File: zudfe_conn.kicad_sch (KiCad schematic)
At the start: 5 parts, among them J1 6469028-1, J2 6469028-1, J3 6469028-1, J4 6469028-1, J5 6469028-1

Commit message: Finish Regulator section
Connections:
- net SFP4.TX_P: now reaches J1.A2
- net SFP5.TX_P: now reaches J1.A3
- net SFP6.TX_P: now reaches J1.A4
- net SFP7.TX_P: now reaches J1.A5
- net SFP4.TX_N: now reaches J1.B2
- net SFP5.TX_N: now reaches J1.B3
- net SFP6.TX_N: now reaches J1.B4
- net SFP7.TX_N: now reaches J1.B5
- net SFP4.RX_P: now reaches J1.C2
- net SFP5.RX_P: now reaches J1.C3
- net SFP6.RX_P: now reaches J1.C4
- net SFP7.RX_P: now reaches J1.C5
- net SFP4.RX_N: now reaches J1.D2
- net SFP5.RX_N: now reaches J1.D3
- net SFP6.RX_N: now reaches J1.D4
- net SFP7.RX_N: now reaches J1.D5
- net SFP0.TX_P: now reaches J3.A6
- net SFP1.TX_P: now reaches J3.A7
- net SFP2.TX_P: now reaches J3.A8
- net SFP3.TX_P: now reaches J3.A9
- net SFP0.TX_N: now reaches J3.B6
- net SFP1.TX_N: now reaches J3.B7
- net SFP2.TX_N: now reaches J3.B8
- net SFP3.TX_N: now reaches J3.B9
- net SFP0.RX_P: now reaches J3.C6
- net SFP1.RX_P: now reaches J3.C7
- net SFP2.RX_P: now reaches J3.C8
- net SFP3.RX_P: now reaches J3.C9
- net SFP0.RX_N: now reaches J3.D6
- net SFP1.RX_N: now reaches J3.D7
- net SFP2.RX_N: now reaches J3.D8
- net SFP3.RX_N: now reaches J3.D9

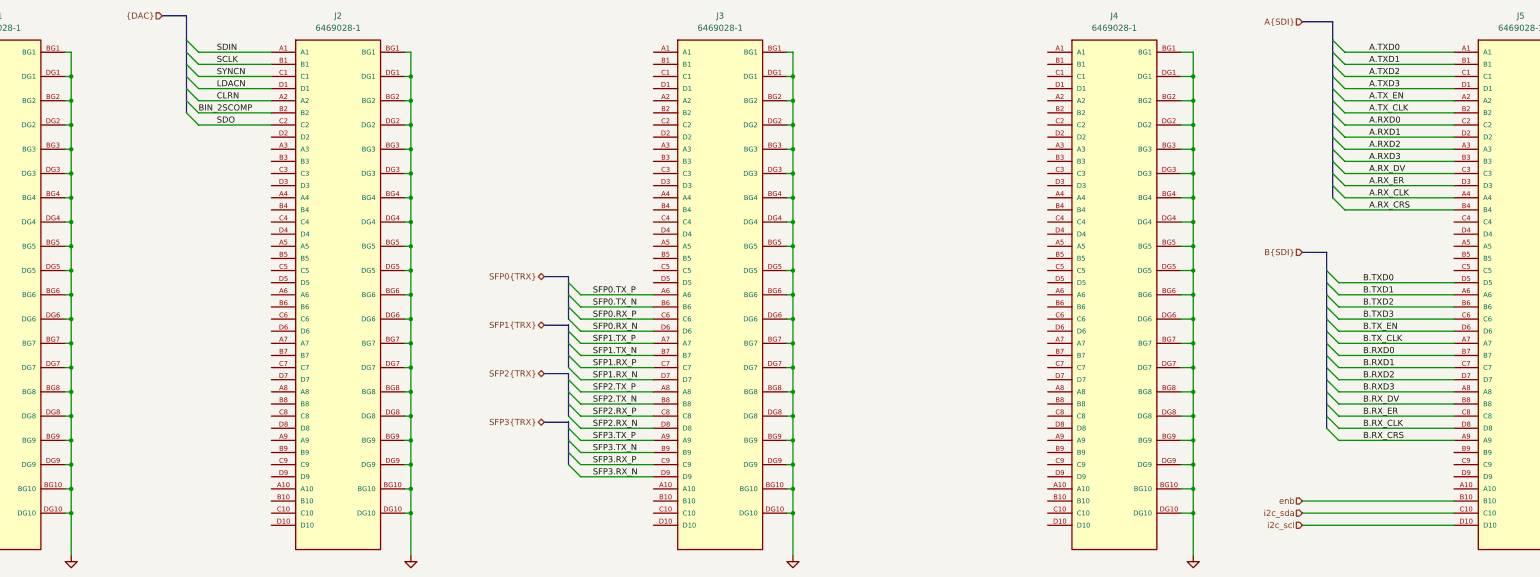
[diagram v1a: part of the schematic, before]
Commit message: Place SFP passives
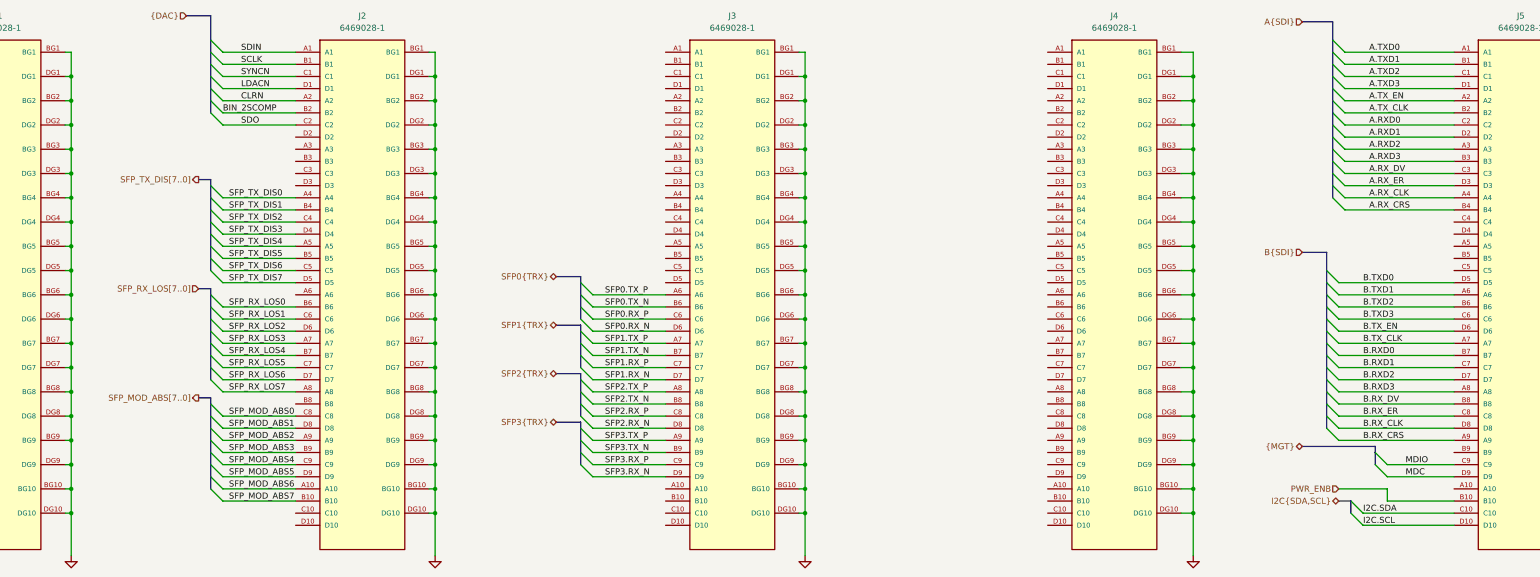
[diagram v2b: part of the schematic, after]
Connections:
- net SFP_MOD_ABS6: now reaches J2.A10
- net SFP_TX_DIS0: now reaches J2.A4
- net SFP_TX_DIS4: now reaches J2.A5
- net SFP_RX_LOS3: now reaches J2.A7
- net SFP_RX_LOS7: now reaches J2.A8
- net SFP_MOD_ABS2: now reaches J2.A9
- net SFP_MOD_ABS7: now reaches J2.B10
- net SFP_TX_DIS1: now reaches J2.B4
- net SFP_TX_DIS5: now reaches J2.B5
- net SFP_RX_LOS0: now reaches J2.B6
- net SFP_RX_LOS4: now reaches J2.B7
- net SFP_MOD_ABS3: now reaches J2.B9
- net SFP_TX_DIS2: now reaches J2.C4
- net SFP_TX_DIS6: now reaches J2.C5
- net SFP_RX_LOS1: now reaches J2.C6
- net SFP_RX_LOS5: now reaches J2.C7
- net SFP_MOD_ABS0: now reaches J2.C8
- net SFP_MOD_ABS4: now reaches J2.C9
- net SFP_TX_DIS3: now reaches J2.D4
- net SFP_TX_DIS7: now reaches J2.D5
- net SFP_RX_LOS2: now reaches J2.D6
- net SFP_RX_LOS6: now reaches J2.D7
- net SFP_MOD_ABS1: now reaches J2.D8
- net SFP_MOD_ABS5: now reaches J2.D9
- net MDIO: now reaches J5.C9
- net MDC: now reaches J5.D9
- net enb renamed PWR_ENB
- net i2c_scl renamed I2C.SCL
- net i2c_sda renamed I2C.SDA
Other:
- moved on the sheet: J2, J3

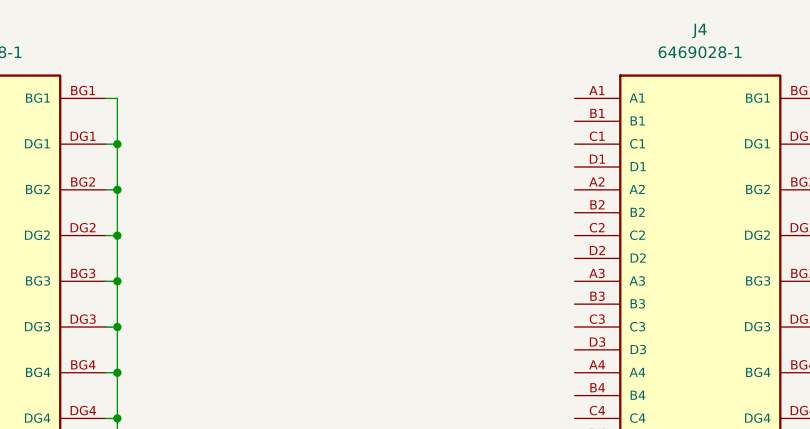
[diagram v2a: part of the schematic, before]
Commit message: Add digital Outputs
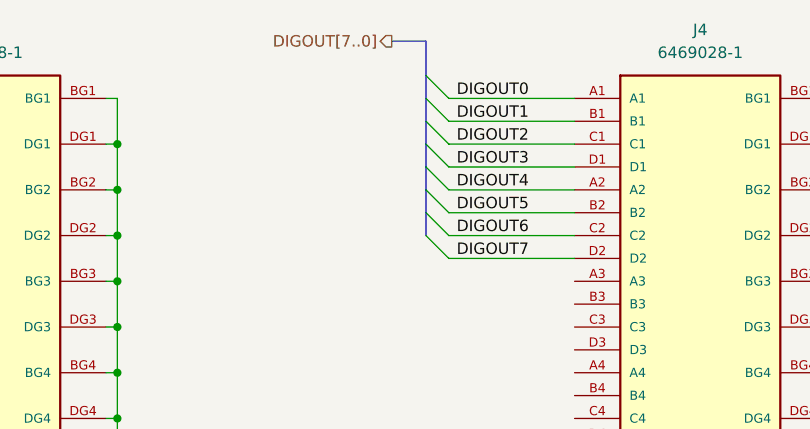
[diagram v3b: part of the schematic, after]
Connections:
- net DIGOUT0: now reaches J4.A1
- net DIGOUT4: now reaches J4.A2
- net DIGOUT1: now reaches J4.B1
- net DIGOUT5: now reaches J4.B2
- net DIGOUT2: now reaches J4.C1
- net DIGOUT6: now reaches J4.C2
- net DIGOUT3: now reaches J4.D1
- net DIGOUT7: now reaches J4.D2
